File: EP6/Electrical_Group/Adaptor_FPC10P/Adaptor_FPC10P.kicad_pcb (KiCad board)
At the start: 2 copper layers, 15.8 x 11.1 mm, 2 parts, among them J1 FPC10P, J3 FPC10P

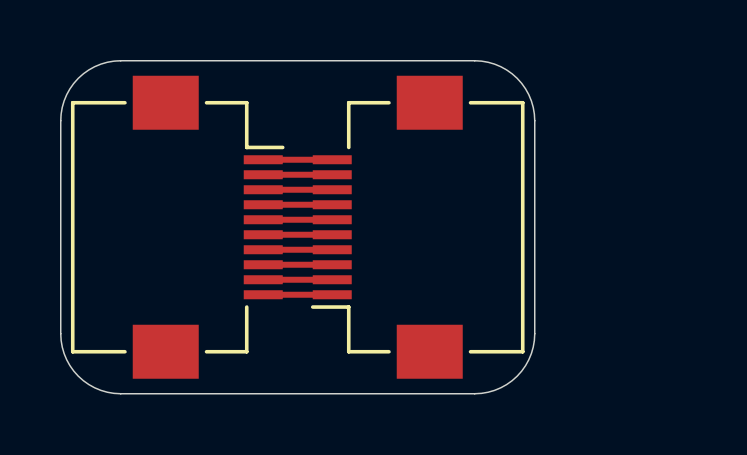
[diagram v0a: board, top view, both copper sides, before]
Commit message: update Adaptor_FPC10P to V1.1
V1.1 move two conns away for 5mm (hard to solder when that close)
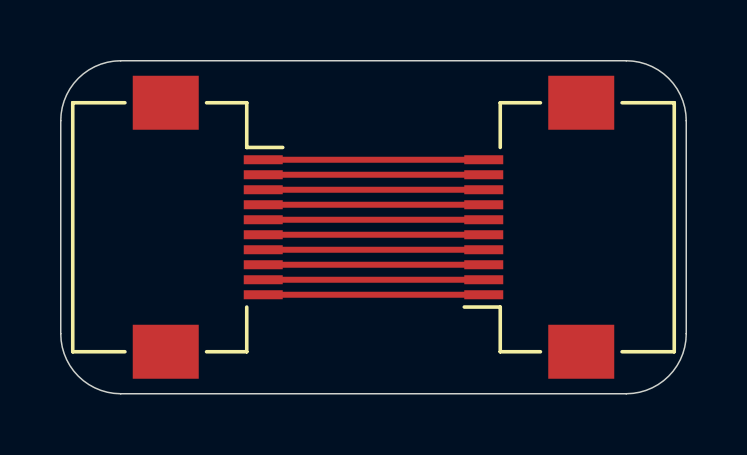
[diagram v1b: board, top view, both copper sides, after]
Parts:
- moved J3 5.05 mm to (126.0, 76.0)
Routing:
- net Net-(J1-Pin_9): track 2.30 -> 7.35 mm
- net Net-(J1-Pin_8): track 2.30 -> 7.35 mm
- net Net-(J1-Pin_7): track 2.30 -> 7.35 mm
- net Net-(J1-Pin_6): track 2.30 -> 7.35 mm
- net Net-(J1-Pin_5): track 2.30 -> 7.35 mm
- net Net-(J1-Pin_4): track 2.30 -> 7.35 mm
- net Net-(J1-Pin_3): track 2.30 -> 7.35 mm
- net Net-(J1-Pin_2): track 2.30 -> 7.35 mm
- net Net-(J1-Pin_10): track 2.30 -> 7.35 mm
- net Net-(J1-Pin_1): track 2.30 -> 7.35 mm
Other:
- board size 15.8 x 11.1 mm -> 20.8 x 11.1 mm
- board text added: "NTUR EP6 Adaptor_FPC10P V1.1 25/06/26 Jack Kuo"
- board text removed: "NTUR EP6 Adaptor V1.0 25/05/05 Jack Kuo"
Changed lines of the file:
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@@
 	(title_block
 		(title "Adaptor_FPC10P")
-		(date "2025-05-05")
-		(rev "1.0")
+		(date "2025-06-26")
+		(rev "1.1")
 		(company "NTURacing")
 		(comment 1 "Jack Kuo")
@@
 	(footprint "Connector_FFC-FPC:Hirose_FH12-10S-0.5SH_1x10-1MP_P0.50mm_Horizontal"
 		(layer "F.Cu")
-		(at 121 76 90)
+		(at 126.05 76 90)
 		(descr "Hirose FH12, FFC/FPC connector, FH12-10S-0.5SH, 10 Pins per row (https://www.hirose.com/product/en/products/FH12/FH12-24S-0.5SH(55)/), generated with kicad-footprint-generator")
 		(tags "connector Hirose FH12 horizontal")
@@
 	(gr_line
 		(start 112.1 70.45)
-		(end 123.9 70.45)
+		(end 128.95 70.45)
 		(stroke
 			(width 0.05)
@@
 	)
 	(gr_line
-		(start 125.9 72.45)
-		(end 125.9 79.55)
+		(start 130.95 72.45)
+		(end 130.95 79.55)
 		(stroke
 			(width 0.05)
@@
 	)
 	(gr_arc
-		(start 123.9 70.45)
-		(mid 125.314214 71.035786)
-		(end 125.9 72.45)
+		(start 128.95 70.45)
+		(mid 130.364214 71.035786)
+		(end 130.95 72.45)
 		(stroke
 			(width 0.05)
@@
 	)
 	(gr_arc
-		(start 125.9 79.55)
-		(mid 125.314214 80.964214)
-		(end 123.9 81.55)
+		(start 130.95 79.55)
+		(mid 130.364214 80.964214)
+		(end 128.95 81.55)
 		(stroke
 			(width 0.05)
@@
 	)
 	(gr_line
-		(start 123.9 81.55)
+		(start 128.95 81.55)
 		(end 112.1 81.55)
 		(stroke
@@
 		(layer "Edge.Cuts")
 	)
-	(gr_text "NTUR\nEP6\nAdaptor\nV1.0 25/05/05\nJack Kuo"
-		(at 123.9 79.55 0)
+	(gr_text "NTUR EP6\nAdaptor_FPC10P\nV1.1 25/06/26\nJack Kuo"
+		(at 125.8 79.2 0)
 		(layer "B.SilkS")
 		(effects
@@
 	(segment
 		(start 116.85 77.25)
-		(end 119.15 77.25)
+		(end 124.2 77.25)
 		(width 0.2)
 		(layer "F.Cu")
@@
 	)
 	(segment
-		(start 116.85 76.75)
-		(end 119.15 76.75)
+		(start 124.2 76.75)
+		(end 116.85 76.75)
 		(width 0.2)
 		(layer "F.Cu")
@@
 	)
 	(segment
-		(start 116.85 75.75)
-		(end 119.15 75.75)
+		(start 124.2 75.75)
+		(end 116.85 75.75)
 		(width 0.2)
 		(layer "F.Cu")
@@
 	)
 	(segment
-		(start 116.85 77.75)
-		(end 119.15 77.75)
+		(start 124.2 77.75)
+		(end 116.85 77.75)
 		(width 0.2)
 		(layer "F.Cu")
@@
 	(segment
 		(start 116.85 73.75)
-		(end 119.15 73.75)
+		(end 124.2 73.75)
 		(width 0.2)
 		(layer "F.Cu")
@@
 	)
 	(segment
-		(start 116.85 74.25)
-		(end 119.15 74.25)
+		(start 124.2 74.25)
+		(end 116.85 74.25)
 		(width 0.2)
 		(layer "F.Cu")
@@
 	(segment
 		(start 116.85 76.25)
-		(end 119.15 76.25)
+		(end 124.2 76.25)
 		(width 0.2)
 		(layer "F.Cu")
@@
 	(segment
 		(start 116.85 74.75)
-		(end 119.15 74.75)
+		(end 124.2 74.75)
 		(width 0.2)
 		(layer "F.Cu")
@@
 	(segment
 		(start 116.85 78.25)
-		(end 119.15 78.25)
+		(end 124.2 78.25)
 		(width 0.2)
 		(layer "F.Cu")
@@
 	(segment
 		(start 116.85 75.25)
-		(end 119.15 75.25)
+		(end 124.2 75.25)
 		(width 0.2)
 		(layer "F.Cu")
